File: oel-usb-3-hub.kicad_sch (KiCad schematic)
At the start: 88 parts, among them J1 USB3_B, J2 USB3_A, J3 USB3_A, J4 USB3_A, J5 USB3_A, U1 TUSB8041, U2 TPS2561, U3 TPS2561, Y1 24MHz

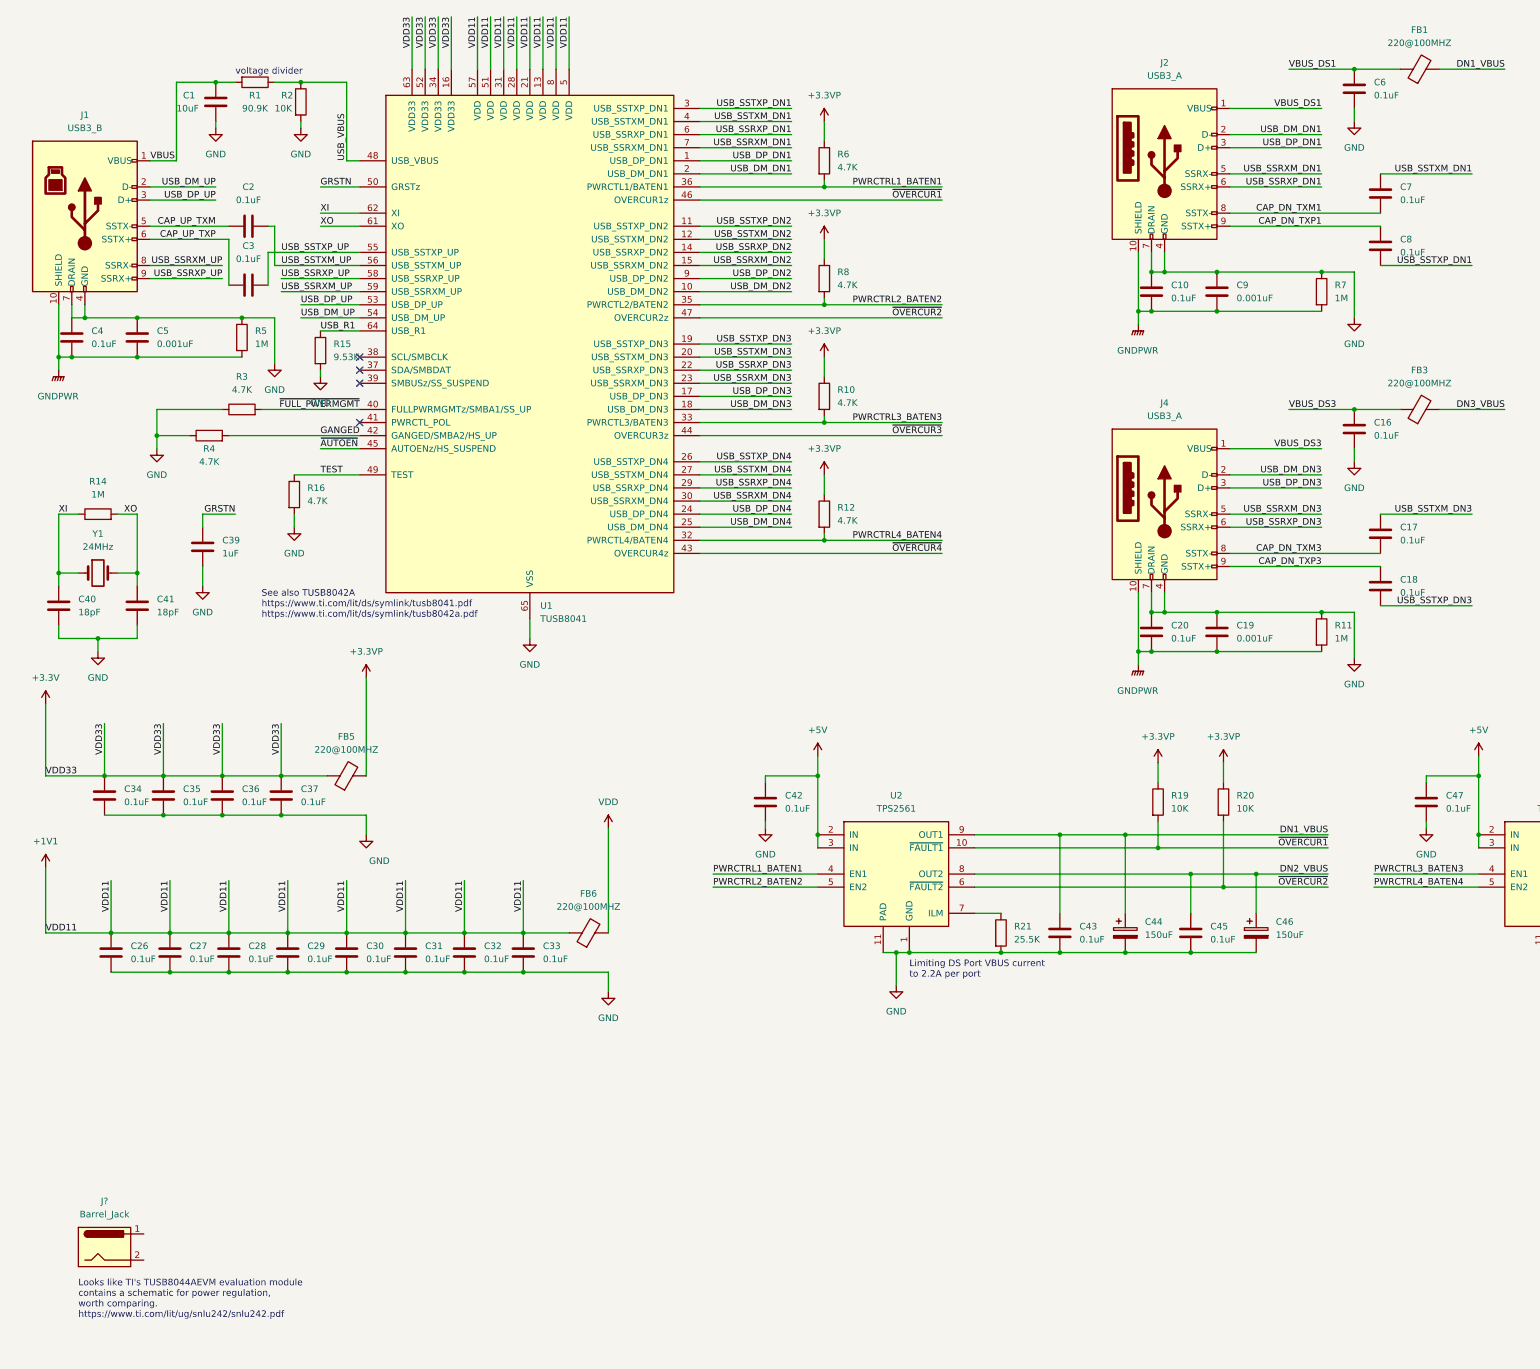
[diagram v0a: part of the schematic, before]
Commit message: Add power to schematic
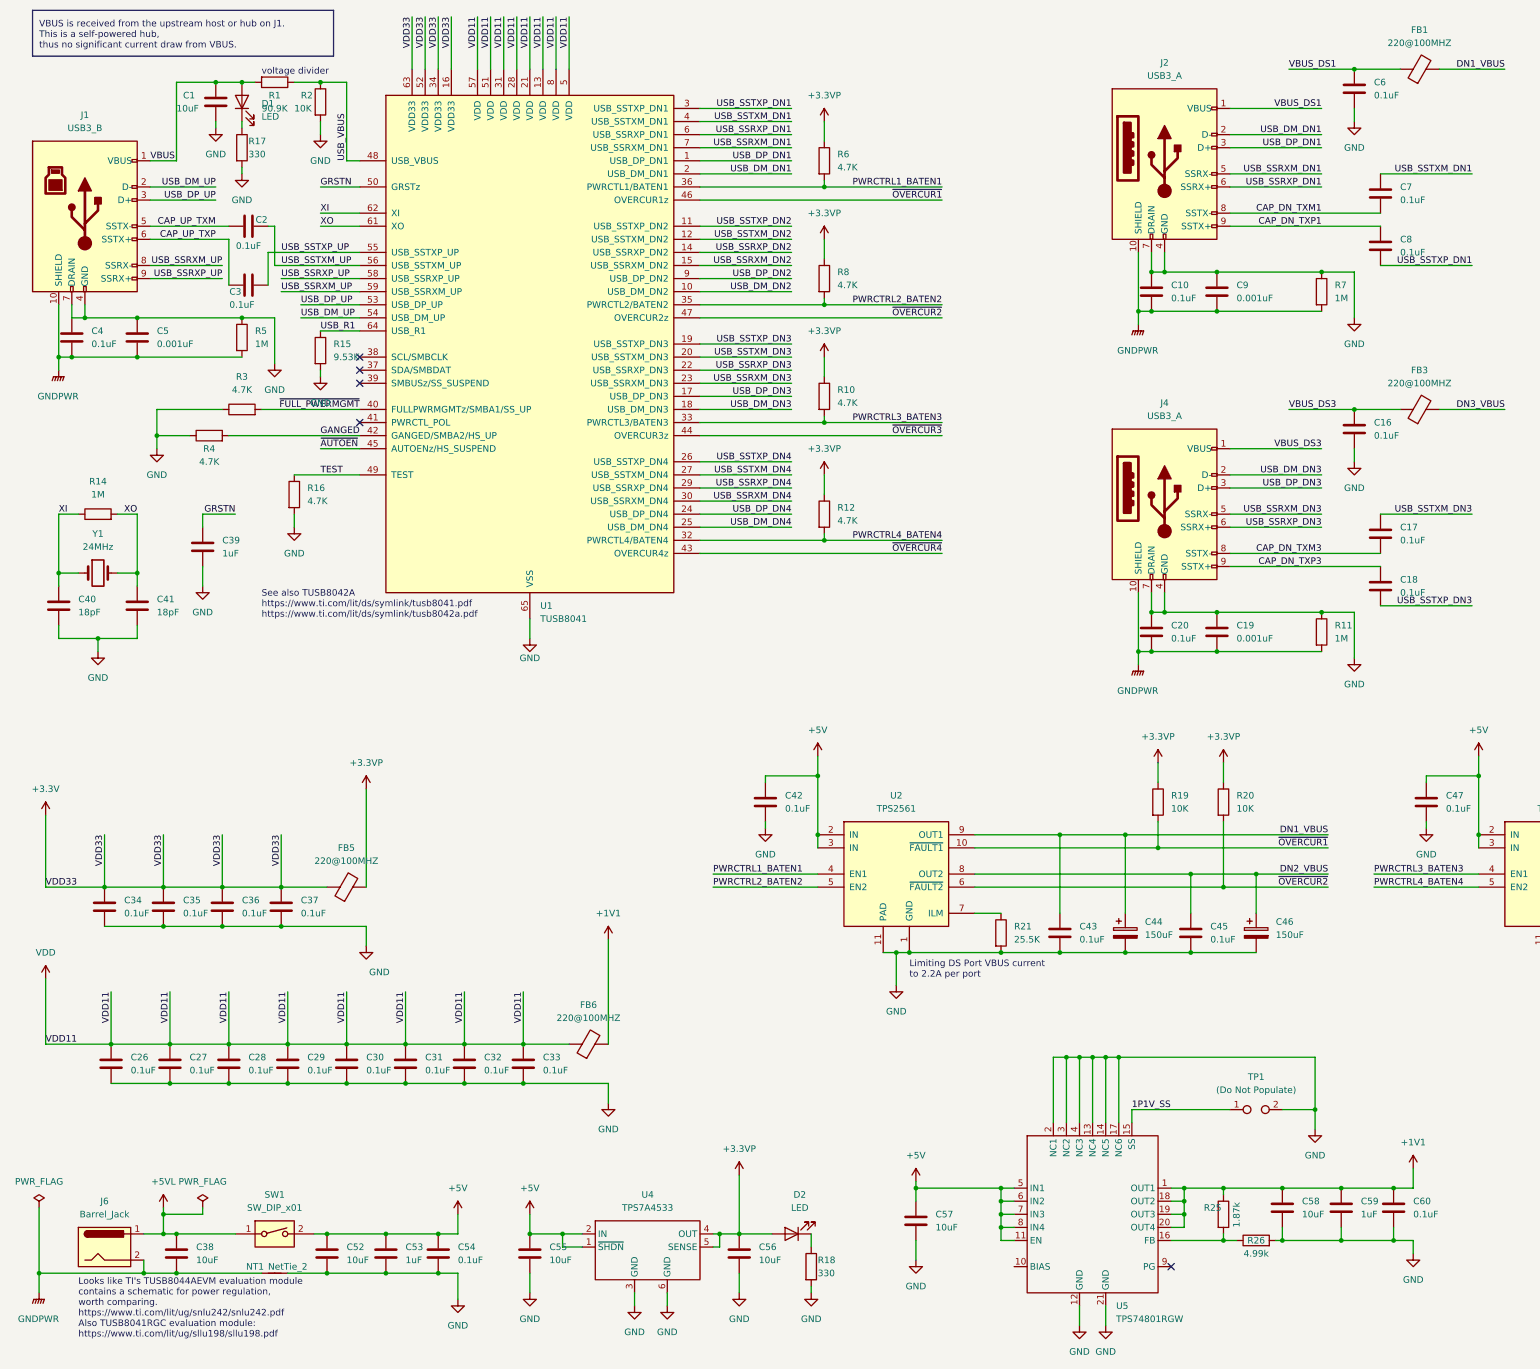
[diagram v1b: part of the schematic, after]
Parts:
- added C38, C52, C55, C56, C57, C58: 10uF, symbol Device:C
- added C53, C59: 1uF, symbol Device:C
- added C54, C60: 0.1uF, symbol Device:C
- added D1, D2: LED, symbol Device:LED
- added NT1: NetTie_2, symbol Device:NetTie_2
- added R17, R18: 330, symbol Device:R
- added R25: 1.87k, symbol Device:R
- added R26: 4.99k, symbol Device:R
- added SW1: SW_DIP_x01, symbol Switch:SW_DIP_x01
- added TP1: (Do Not Populate), symbol Connector:TestPoint_2Pole
- added U4: TPS7A4533, symbol tps:TPS7A4533
- added U5: TPS74801RGW, symbol tps:TPS74801RGW
- gave numbers to parts that had none: 1
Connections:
- net +1V1: now also FB6.2, C58.1, C59.1, C60.1, R25.1, U5.1 (OUT1), U5.18 (OUT2), U5.19 (OUT3), U5.20 (OUT4); no longer C26.1, C27.1, C28.1, C29.1, C30.1, C31.1, C32.1, C33.1, FB6.1, U1.13 (VDD), U1.21 (VDD), U1.28 (VDD), U1.31 (VDD), U1.5 (VDD), U1.51 (VDD), U1.57 (VDD), U1.8 (VDD)
- net +3.3VP: now also C56.1, D2.2 (A), U4.4 (OUT), U4.5 (SENSE)
- net +5V: now also C52.1, C53.1, C54.1, C55.1, C57.1, SW1.2, U4.1 (~{SHDN}), U4.2 (IN), U5.11 (EN), U5.5 (IN1), U5.6 (IN2), U5.7 (IN3), U5.8 (IN4)
- net GND: now also C52.2, C53.2, C54.2, C55.2, C56.2, C57.2, C58.2, C59.2, C60.2, NT1.2, R17.2, R18.2, R26.2, TP1.2, U4.3 (GND), U4.6 (GND), U5.12 (GND), U5.13 (NC4), U5.14 (NC5), U5.17 (NC6), U5.2 (NC1), U5.21 (GND), U5.3 (NC2), U5.4 (NC3)
- net GNDPWR: now also J6.2, C38.2, NT1.1
- net VBUS: now also D1.2 (A)
- net VDD: now also C26.1, C27.1, C28.1, C29.1, C30.1, C31.1, C32.1, C33.1, FB6.1, U1.13 (VDD), U1.21 (VDD), U1.28 (VDD), U1.31 (VDD), U1.5 (VDD), U1.51 (VDD), U1.57 (VDD), U1.8 (VDD); no longer FB6.2
- net +5VL: now reaches J6.1
- net +5VL: now also C38.1, SW1.1
- new net: R25.2, R26.1, U5.16 (FB)
- new net: D2.1 (K), R18.1
- new net: D1.1 (K), R17.1
- new net 1P1V_SS: TP1.1, U5.15 (SS)
- no-connect marks 4 -> 5
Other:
- note added: "Looks like TI's TUSB8044AEVM evaluation module contains a schematic for power regulation, worth comparing. https://www.ti.com/lit/ug/snlu242/snlu242.pdf Also TUSB8041RGC evaluation module: https://www.ti.com/lit/ug/sllu198/sllu198.pdf"
- note added: "VBUS is received from the upstream host or hub on J1. This is a self-powered hub, thus no significant current draw from VBUS."
- note removed: "Looks like TI's TUSB8044AEVM evaluation module contains a schematic for power regulation, worth comparing. https://www.ti.com/lit/ug/snlu242/snlu242.pdf"
- moved on the sheet: C26, C27, C28, C29, C30, C31, C32, C33, C34, C35, C36, C37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

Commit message: First sketch of PCB layout
Looks like some pieces may need to be mounted to the bottom of the PCB.
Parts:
- removed J1: USB3_B, symbol Connector:USB3_B
- added J1: USB3_B_Micro, Connector_USB:USB3_Micro-B_Connfly_DS1104-01, symbol Connector:USB3_B_Micro
- C1, C10, C11, C12, C13, C14, C15, C16, C17, C18, C19, C2, C20, C21, C22, C23, C24, C25, C26, C27, C28, C29, C3, C30, C31, C32, C33, C34, C35, C36, C37, C38, C39, C4, C40, C41, C42, C43, C44, C45, C46, C47, C48, C49, C5, C50, C51, C52, C53, C54, C55, C56, C57, C58, C59, C6, C60, C7, C8, C9: footprint (none) -> Capacitor_SMD:C_0603_1608Metric_Pad1.08x0.95mm_HandSolder
- D1, D2: footprint (none) -> Diode_SMD:D_0603_1608Metric_Pad1.05x0.95mm_HandSolder
- FB1, FB2, FB3, FB4, FB5, FB6: value 220@100MHZ -> BLM18PG221SN1D 220@100MHZ; footprint (none) -> Resistor_SMD:R_0603_1608Metric_Pad0.98x0.95mm_HandSolder
- J2, J3, J4, J5: footprint (none) -> Connector_USB:USB3_A_Molex_48393-001
- J6: footprint (none) -> Connector_BarrelJack:BarrelJack_Horizontal
- NT1: footprint (none) -> NetTie:NetTie-2_SMD_Pad2.0mm
- R1, R10, R11, R12, R13, R14, R15, R16, R17, R18, R19, R2, R20, R21, R22, R23, R24, R25, R26, R3, R4, R5, R6, R7, R8, R9, TP1: footprint (none) -> Resistor_SMD:R_0603_1608Metric_Pad0.98x0.95mm_HandSolder
- SW1: footprint (none) -> Button_Switch_THT:SW_DIP_SPSTx01_Slide_6.7x4.1mm_W7.62mm_P2.54mm_LowProfile
- U4: footprint (none) -> Package_TO_SOT_SMD:SOT-223-6_TabPin3
- U5: footprint (none) -> Package_DFN_QFN:Texas_S-PVQFN-N20_EP3.15x3.15mm_ThermalVias
- Y1: footprint (none) -> Crystal:Crystal_HC49-U_Vertical
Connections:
- net CAP_UP_TXM: now also J1.6 (SSTX-)
- net CAP_UP_TXP: now also J1.7 (SSTX+)
- net GND: now also J1.5 (GND), J1.8 (DRAIN)
- net GNDPWR: now also J1.11 (SHIELD)
- net USB_DM_UP: now also J1.2 (D-)
- net USB_DP_UP: now also J1.3 (D+)
- net USB_SSRXM_UP: now also J1.9 (SSRX-)
- net USB_SSRXP_UP: now also J1.10 (SSRX+)
- net VBUS: now also J1.1 (VBUS)
- net +3V3 renamed +3.3V
- new net (OTG): J1.4 (ID)
- no-connect marks 5 -> 7
